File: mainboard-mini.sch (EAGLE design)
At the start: 103 parts, among them IC1 XC6206P332MR, IC2 LM2901, IC3 NC7SZ10P6X, IC4 STM32F103RBT6, IC5 TDA2822D, IC6 SN65HVD230, IC7 RT8259GE, Q1 8MHz

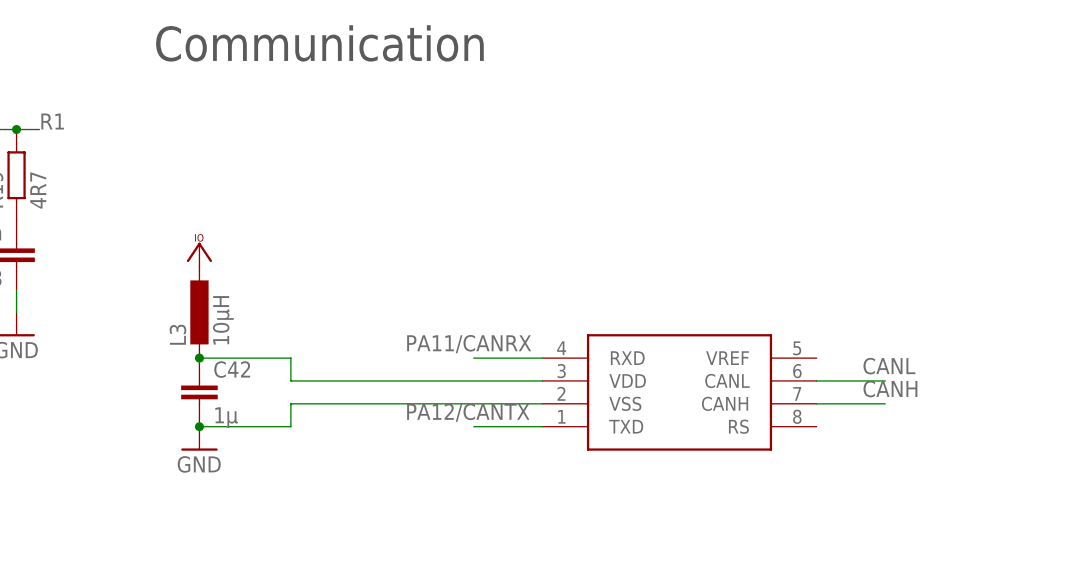
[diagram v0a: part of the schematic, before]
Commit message: Added 10k resistor to CAN transceiver RS pin
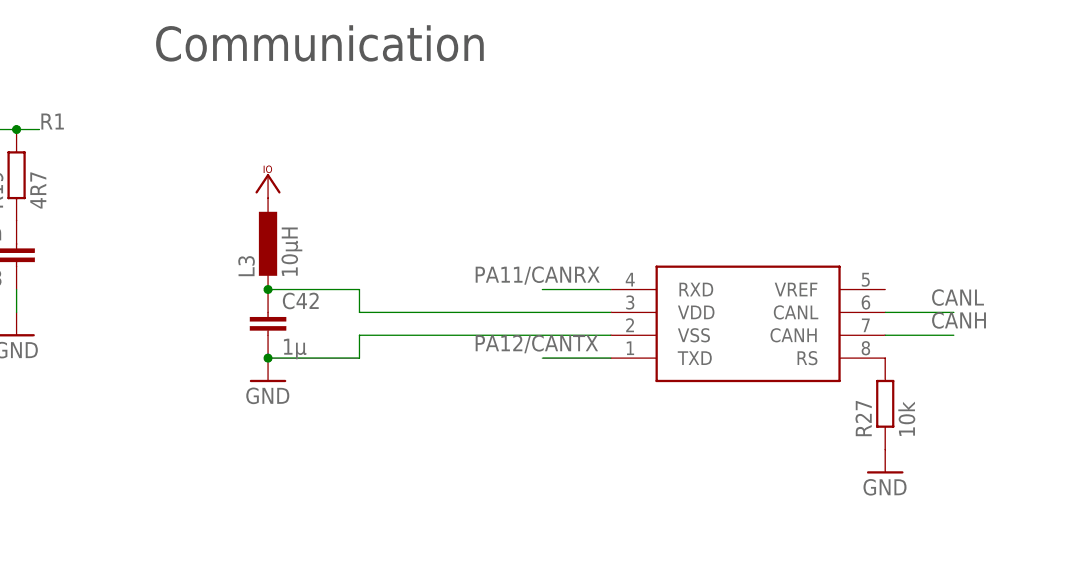
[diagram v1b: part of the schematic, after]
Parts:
- added R27: 10k, rcl:R-EU_R0603
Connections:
- new net N$24: IC6.RS, R27.2
- net GND: now also R27.1
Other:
- moved on the sheet: C42, L3
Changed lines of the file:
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@@
 <part name="C2" library="rcl" deviceset="C-EU" device="C0603" value="10µ"/>
 <part name="SJ3" library="SparkFun-Passives" deviceset="SOLDERJUMPER_2WAY" device="PASTE2&amp;3"/>
+<part name="R27" library="rcl" deviceset="R-EU_" device="R0603" value="10k"/>
+<part name="GND1" library="supply1" deviceset="GND" device=""/>
 </parts>
 <sheets>
@@
 <instance part="C44" gate="G$1" x="-124.46" y="-99.06"/>
 <instance part="C45" gate="G$1" x="-63.5" y="-99.06"/>
-<instance part="IC6" gate="G$1" x="213.36" y="-91.44" rot="MR180"/>
+<instance part="IC6" gate="G$1" x="220.98" y="-83.82" rot="MR180"/>
 <instance part="GND31" gate="1" x="-71.12" y="-71.12"/>
 <instance part="C32" gate="G$1" x="-71.12" y="-63.5"/>
@@
 <instance part="D1" gate="G$1" x="0" y="127" rot="R270"/>
 <instance part="P+12" gate="1" x="0" y="134.62" smashed="yes"/>
-<instance part="L3" gate="G$1" x="165.1" y="-86.36"/>
+<instance part="L3" gate="G$1" x="172.72" y="-78.74"/>
 <instance part="FID1" gate="G$1" x="-97.79" y="119.38"/>
 <instance part="P+15" gate="VCC" x="-68.58" y="109.22"/>
@@
 <instance part="P+9" gate="VCC" x="223.52" y="-7.62" smashed="yes"/>
 <instance part="GND2" gate="1" x="83.82" y="0" rot="MR0"/>
-<instance part="C42" gate="G$1" x="165.1" y="-93.98"/>
-<instance part="GND4" gate="1" x="165.1" y="-101.6"/>
+<instance part="C42" gate="G$1" x="172.72" y="-86.36"/>
+<instance part="GND4" gate="1" x="172.72" y="-93.98"/>
 <instance part="LOGO1" gate="G$1" x="193.04" y="119.38"/>
 <instance part="IC3" gate="&gt;NAME" x="246.38" y="-5.08" smashed="yes">
@@
 <instance part="R5" gate="G$1" x="43.18" y="109.22" rot="R90"/>
 <instance part="R4" gate="G$1" x="60.96" y="111.76" rot="R180"/>
-<instance part="VCC5" gate="G$1" x="165.1" y="-78.74" smashed="yes" rot="MR0"/>
+<instance part="VCC5" gate="G$1" x="172.72" y="-71.12" smashed="yes" rot="MR0"/>
 <instance part="J1" gate="G$1" x="7.62" y="68.58" rot="R90"/>
 <instance part="R16" gate="G$1" x="66.04" y="-63.5"/>
@@
 <instance part="C2" gate="G$1" x="0" y="121.92"/>
 <instance part="SJ3" gate="G$1" x="-35.56" y="20.32" rot="R270"/>
+<instance part="R27" gate="G$1" x="241.3" y="-96.52" rot="R90"/>
+<instance part="GND1" gate="1" x="241.3" y="-104.14"/>
 </instances>
 <busses>
@@
 <segment>
 <pinref part="IC6" gate="G$1" pin="RXD"/>
-<wire x1="203.2" y1="-91.44" x2="195.58" y2="-91.44" width="0.1524" layer="91"/>
-<label x="187.96" y="-88.9" size="1.778" layer="95" rot="MR180"/>
+<wire x1="210.82" y1="-83.82" x2="203.2" y2="-83.82" width="0.1524" layer="91"/>
+<label x="195.58" y="-81.28" size="1.778" layer="95" rot="MR180"/>
 </segment>
 </net>
@@
 <segment>
 <pinref part="IC6" gate="G$1" pin="TXD"/>
-<wire x1="203.2" y1="-99.06" x2="195.58" y2="-99.06" width="0.1524" layer="91"/>
-<label x="187.96" y="-96.52" size="1.778" layer="95" rot="MR180"/>
+<wire x1="210.82" y1="-91.44" x2="203.2" y2="-91.44" width="0.1524" layer="91"/>
+<label x="195.58" y="-88.9" size="1.778" layer="95" rot="MR180"/>
 </segment>
 </net>
@@
 <pinref part="C42" gate="G$1" pin="2"/>
 <pinref part="IC6" gate="G$1" pin="VSS"/>
-<wire x1="203.2" y1="-96.52" x2="175.26" y2="-96.52" width="0.1524" layer="91"/>
-<wire x1="175.26" y1="-96.52" x2="175.26" y2="-99.06" width="0.1524" layer="91"/>
-<wire x1="175.26" y1="-99.06" x2="165.1" y2="-99.06" width="0.1524" layer="91"/>
-<junction x="165.1" y="-99.06"/>
+<wire x1="210.82" y1="-88.9" x2="182.88" y2="-88.9" width="0.1524" layer="91"/>
+<wire x1="182.88" y1="-88.9" x2="182.88" y2="-91.44" width="0.1524" layer="91"/>
+<wire x1="182.88" y1="-91.44" x2="172.72" y2="-91.44" width="0.1524" layer="91"/>
+<junction x="172.72" y="-91.44"/>
 </segment>
 <segment>
@@
 <wire x1="-35.56" y1="86.36" x2="-35.56" y2="78.74" width="0.1524" layer="91"/>
 <pinref part="JP2" gate="A" pin="1"/>
+</segment>
+<segment>
+<pinref part="R27" gate="G$1" pin="1"/>
+<pinref part="GND1" gate="1" pin="GND"/>
 </segment>
 </net>
@@
 <segment>
 <pinref part="IC6" gate="G$1" pin="CANL"/>
-<wire x1="233.68" y1="-93.98" x2="241.3" y2="-93.98" width="0.1524" layer="91"/>
-<label x="238.76" y="-91.44" size="1.778" layer="95" rot="MR180"/>
+<wire x1="241.3" y1="-86.36" x2="248.92" y2="-86.36" width="0.1524" layer="91"/>
+<label x="246.38" y="-83.82" size="1.778" layer="95" rot="MR180"/>
 </segment>
 <segment>
@@
 <segment>
 <pinref part="IC6" gate="G$1" pin="CANH"/>
-<wire x1="233.68" y1="-96.52" x2="241.3" y2="-96.52" width="0.1524" layer="91"/>
-<label x="238.76" y="-93.98" size="1.778" layer="95" rot="MR180"/>
+<wire x1="241.3" y1="-88.9" x2="248.92" y2="-88.9" width="0.1524" layer="91"/>
+<label x="246.38" y="-86.36" size="1.778" layer="95" rot="MR180"/>
 </segment>
 <segment>
@@
 <pinref part="L3" gate="G$1" pin="2"/>
 <pinref part="IC6" gate="G$1" pin="VDD"/>
-<wire x1="203.2" y1="-93.98" x2="175.26" y2="-93.98" width="0.1524" layer="91"/>
-<wire x1="175.26" y1="-93.98" x2="175.26" y2="-91.44" width="0.1524" layer="91"/>
-<wire x1="175.26" y1="-91.44" x2="165.1" y2="-91.44" width="0.1524" layer="91"/>
-<junction x="165.1" y="-91.44"/>
+<wire x1="210.82" y1="-86.36" x2="182.88" y2="-86.36" width="0.1524" layer="91"/>
+<wire x1="182.88" y1="-86.36" x2="182.88" y2="-83.82" width="0.1524" layer="91"/>
+<wire x1="182.88" y1="-83.82" x2="172.72" y2="-83.82" width="0.1524" layer="91"/>
+<junction x="172.72" y="-83.82"/>
 </segment>
 </net>
@@
 </segment>
 </net>
+<net name="N$24" class="0">
+<segment>
+<pinref part="IC6" gate="G$1" pin="RS"/>
+<pinref part="R27" gate="G$1" pin="2"/>
+</segment>
+</net>
